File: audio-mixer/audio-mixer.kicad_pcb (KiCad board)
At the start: 2 copper layers, 72.5 x 151.2 mm, 57 parts, among them J1 Input A1, J10 Pot, J11 Input B3, J12 Pot, J13 Pot, J14 Output A, J15 Pot, J16 Output B, J17 AudioJack4, J18 Power, J19 Power, J2 Pot, J20 Power, J3 Input A2, J4 Pot, J5 Input A3, J6 Pot, J7 Input B1, J8 Pot, J9 Input B2, SW1 Mono/Stereo, U1 TL074

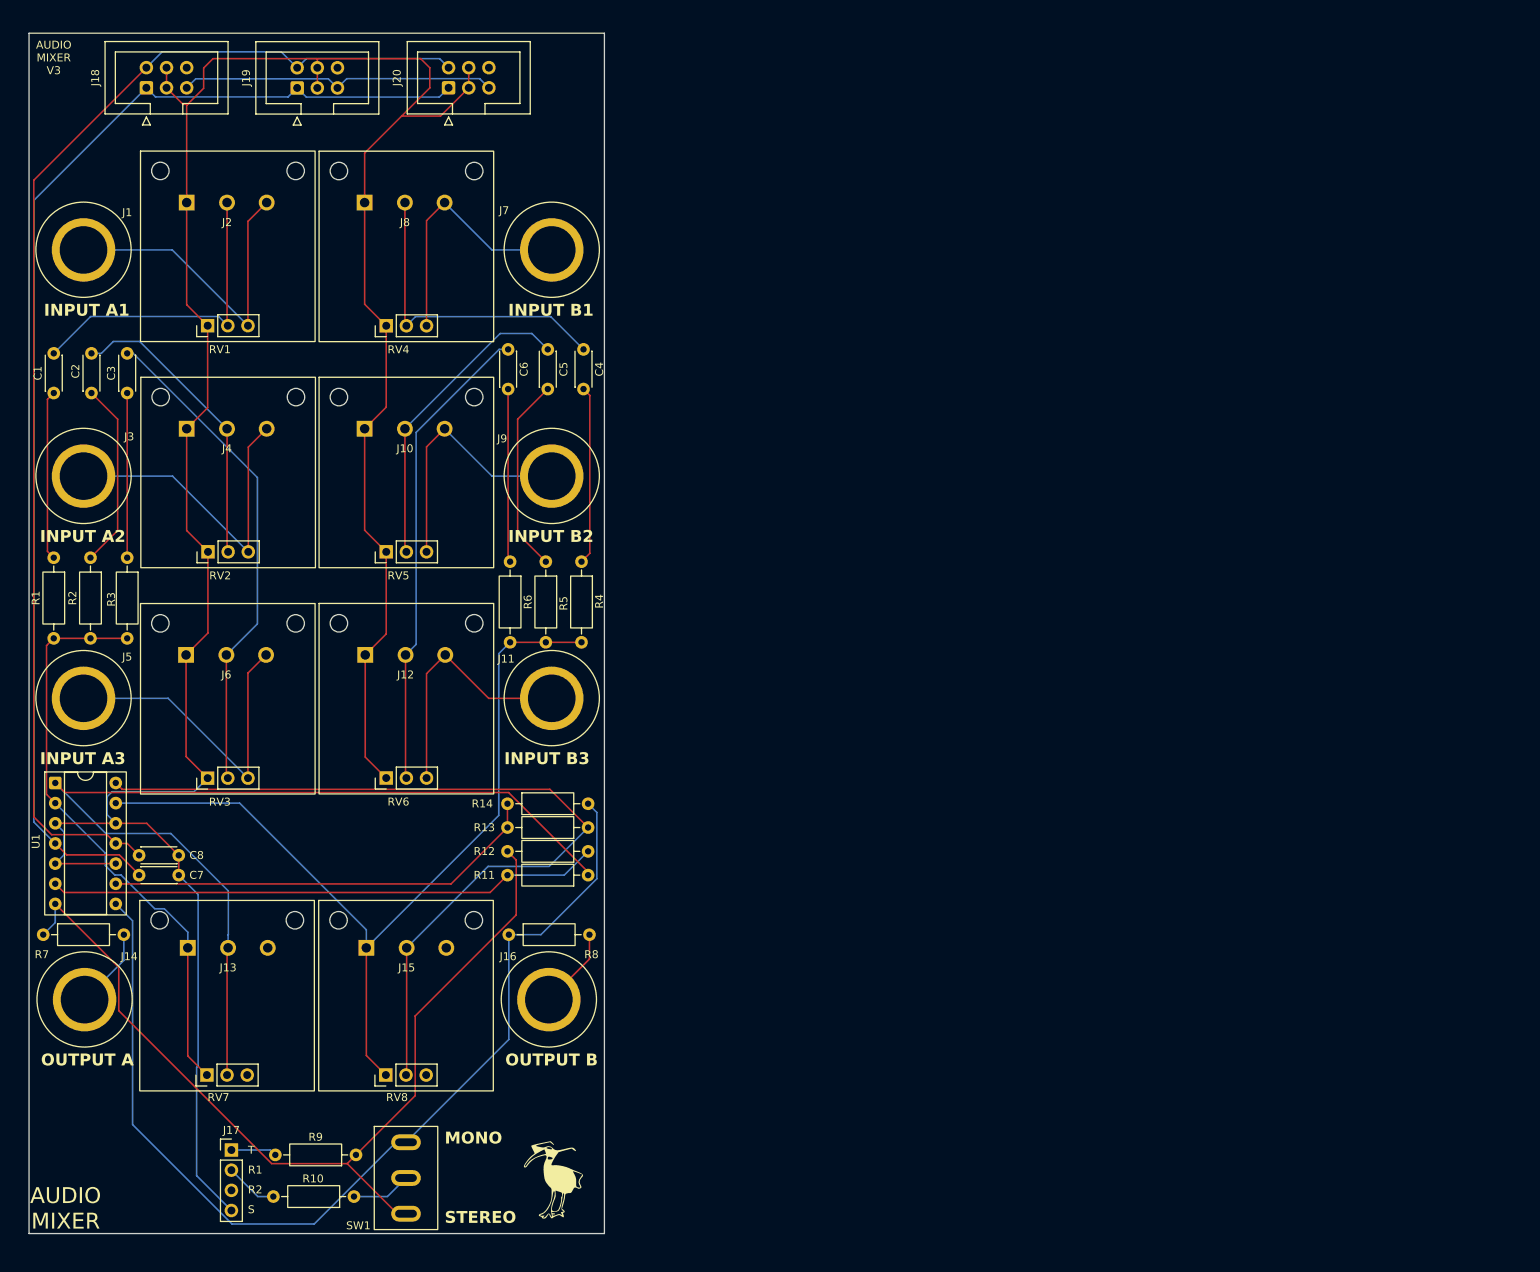
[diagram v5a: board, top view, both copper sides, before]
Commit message: Update audio mixer to new format
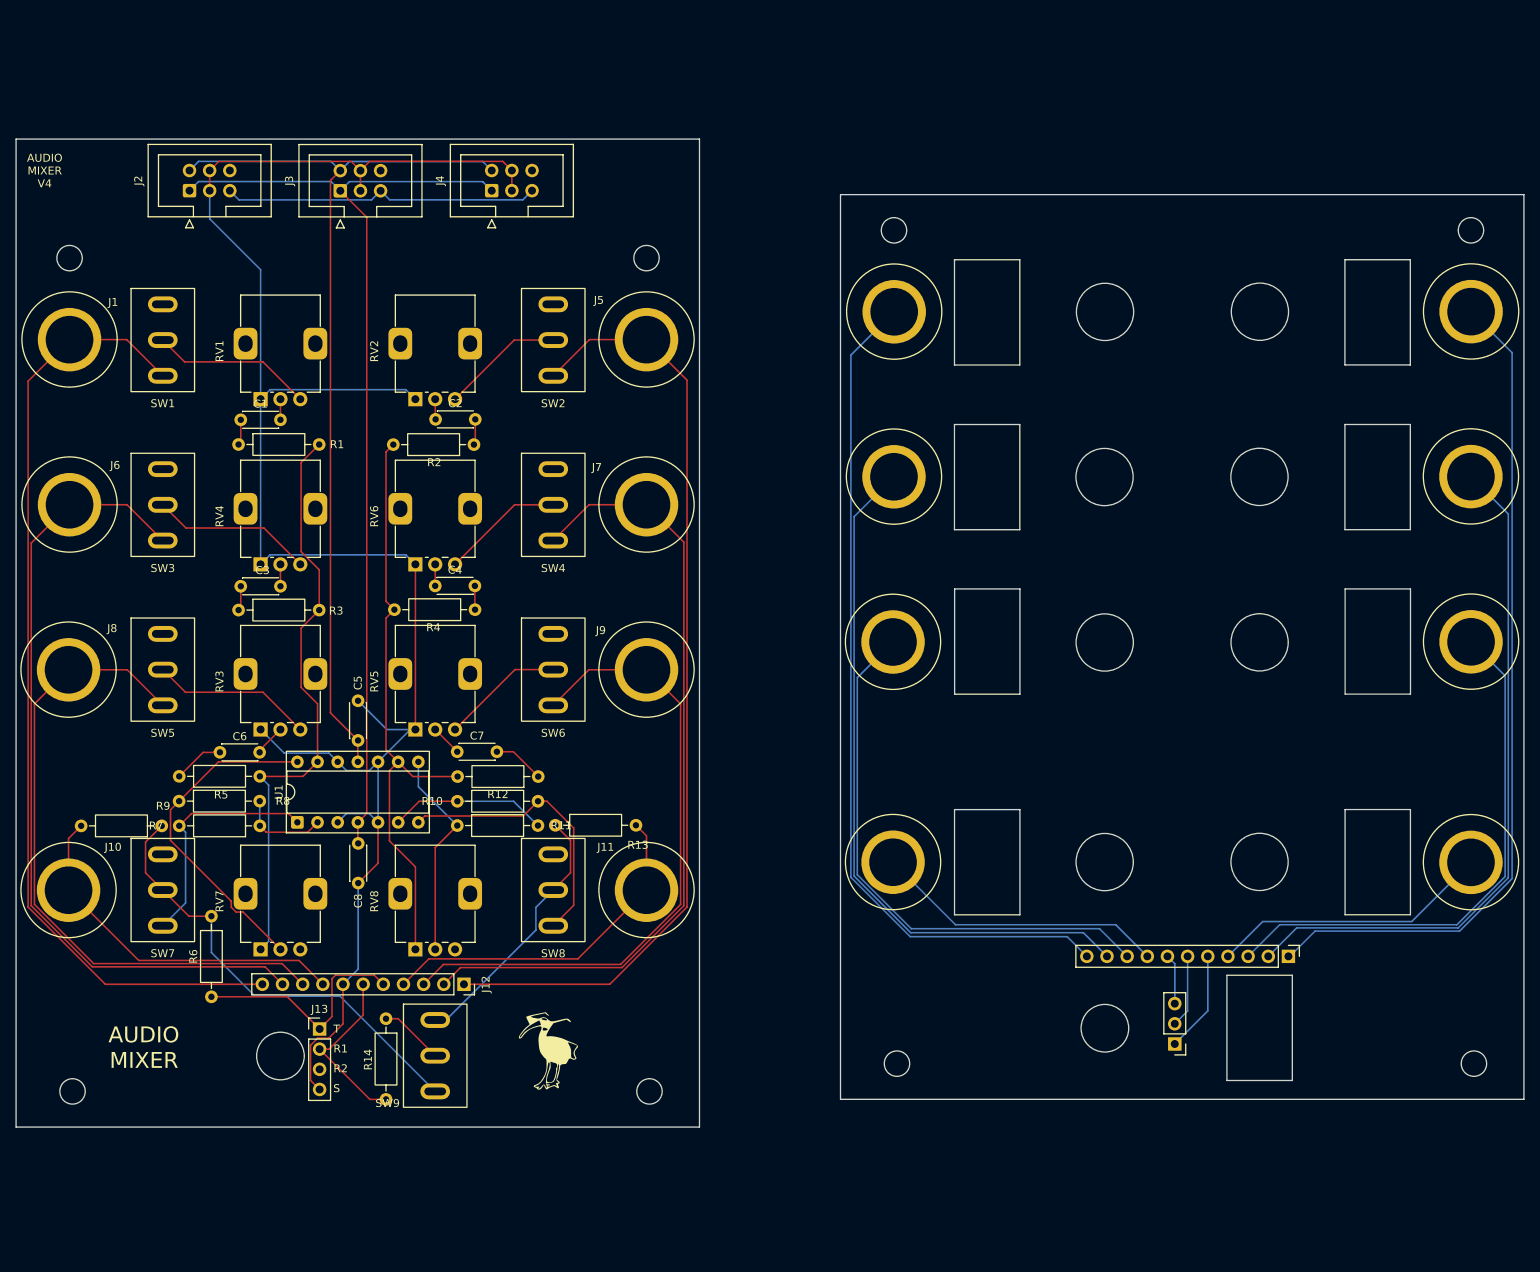
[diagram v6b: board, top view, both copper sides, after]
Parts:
- removed F1, F2, F3, F4: foot, modular2:foot
- removed the J10 at (78.0, 77.5)
- removed the J13 at (55.7, 142.9)
- removed the J2 at (55.6, 49.0)
- removed the J4 at (55.6, 77.5)
- removed the J6 at (55.5, 106.0)
- removed the J8 at (78.0, 49.0)
- added J14: Input A1, modular2:banana-jack, F.Cu at (139.7, 59.7)
- added J16: Input A2, modular2:banana-jack, F.Cu at (139.6, 80.5)
- added J17: Input B2, modular2:banana-jack, F.Cu at (212.3, 80.5)
- added J18: Input A3, modular2:banana-jack, F.Cu at (139.5, 101.3)
- added J19: Input B3, modular2:banana-jack, F.Cu at (212.3, 101.3)
- added J20: Output A, modular2:banana-jack, F.Cu at (139.5, 129.1)
- added J21: Output B, modular2:banana-jack, F.Cu at (212.3, 129.1)
- added J22: Conn_01x11_Pin, Connector_PinHeader_2.54mm:PinHeader_1x11_P2.54mm_Vertical, F.Cu at (189.3, 141.0)
- added J23: Conn_01x03_Pin, Connector_PinHeader_2.54mm:PinHeader_1x03_P2.54mm_Vertical, F.Cu at (175.0, 152.0)
- added REF**: MountingHole_3.2mm_M3, MountingHole:MountingHole_3.2mm_M3, F.Cu at (108.8, 158.0)
- added REF**: MountingHole_3.2mm_M3, MountingHole:MountingHole_3.2mm_M3, F.Cu at (139.6, 49.5)
- added REF**: MountingHole_3.2mm_M3, MountingHole:MountingHole_3.2mm_M3, F.Cu at (212.3, 49.5)
- added REF**: MountingHole_3.2mm_M3, MountingHole:MountingHole_3.2mm_M3, F.Cu at (35.7, 53.0)
- added REF**: MountingHole_3.2mm_M3, MountingHole:MountingHole_3.2mm_M3, F.Cu at (140.0, 154.5)
- added REF**: MountingHole_3.2mm_M3, MountingHole:MountingHole_3.2mm_M3, F.Cu at (108.4, 53.0)
- added REF**: MountingHole_3.2mm_M3, MountingHole:MountingHole_3.2mm_M3, F.Cu at (212.7, 154.5)
- added REF**: MountingHole_3.2mm_M3, MountingHole:MountingHole_3.2mm_M3, F.Cu at (36.1, 158.0)
- added SW1: Iso A1, modular2:switch1, F.Cu at (47.5, 63.3)
- added SW2: Iso B1, modular2:switch1, F.Cu at (96.7, 63.3)
- added SW3: Iso A2, modular2:switch1, F.Cu at (47.5, 84.1)
- added SW4: Iso B2, modular2:switch1, F.Cu at (96.7, 84.1)
- added SW5: Iso A3, modular2:switch1, F.Cu at (47.5, 104.8)
- added SW6: Iso B3, modular2:switch1, F.Cu at (96.7, 104.8)
- added SW7: Iso A, modular2:switch1, F.Cu at (47.5, 132.6)
- added SW8: Iso B, modular2:switch1, F.Cu at (96.7, 132.6)
- J12: value Pot -> Conn_01x11_Socket; footprint modular2:pot -> Connector_PinSocket_2.54mm:PinSocket_1x11_P2.54mm_Vertical
- J15: value Pot -> Input B1; footprint modular2:pot -> modular2:banana-jack
- RV1: value 100K -> 100K - A1; footprint modular2:pot-socket -> modular2:Potentiometer_Alps_RK09K_Single_Vertical - knob padding
- RV2: renamed from RV4; value 100K -> 100K - B1; footprint modular2:pot-socket -> modular2:Potentiometer_Alps_RK09K_Single_Vertical - knob padding
- RV3: value 100K -> 100K - A3; footprint modular2:pot-socket -> modular2:Potentiometer_Alps_RK09K_Single_Vertical - knob padding
- RV4: renamed from RV2; value 100K -> 100K - A2; footprint modular2:pot-socket -> modular2:Potentiometer_Alps_RK09K_Single_Vertical - knob padding
- RV5: renamed from RV6; value 100K -> 100K - B3; footprint modular2:pot-socket -> modular2:Potentiometer_Alps_RK09K_Single_Vertical - knob padding
- RV6: renamed from RV5; value 100K -> 100K - B2; footprint modular2:pot-socket -> modular2:Potentiometer_Alps_RK09K_Single_Vertical - knob padding
- RV7: value 100K -> 100K - A; footprint modular2:pot-socket -> modular2:Potentiometer_Alps_RK09K_Single_Vertical - knob padding
- RV8: value 100K -> 100K - B; footprint modular2:pot-socket -> modular2:Potentiometer_Alps_RK09K_Single_Vertical - knob padding
- moved J15 157.8 mm to (212.3, 59.7)
- moved C6 53.0 mm to (59.7, 115.3), turned to 180 degrees
- moved R8 52.4 mm to (49.5, 121.4), turned to 0 degrees
- moved C7 51.1 mm to (84.6, 115.2), turned to 0 degrees
- moved R7 41.5 mm to (59.7, 124.5)
- moved J12 39.2 mm to (85.4, 144.5), turned to -90 degrees
- moved C3 37.8 mm to (62.3, 94.3), turned to 180 degrees
- moved R6 35.2 mm to (53.6, 135.9), turned to -90 degrees
- moved C4 33.0 mm to (81.8, 94.3), turned to 0 degrees
- moved U1 30.9 mm to (64.4, 124.1), turned to 90 degrees
- moved C5 29.8 mm to (72.1, 108.8), turned to -90 degrees
- moved C1 29.8 mm to (62.3, 73.4), turned to 180 degrees
- moved R5 28.3 mm to (49.6, 118.3), turned to 0 degrees
- moved R1 27.3 mm to (57.0, 76.5), turned to 0 degrees
- moved R12 27.3 mm to (94.8, 118.3), turned to 180 degrees
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- renumbered C4 to C2, C2 to C3, C5 to C4, C8 to C5, C3 to C6, C6 to C7, C7 to C8, J14 to J10, J16 to J11, J17 to J13, J18 to J2, J19 to J3, J20 to J4, J7 to J5, J3 to J6, J9 to J7, J5 to J8, J11 to J9, R14 to R10, R13 to R11, R6 to R12, R8 to R13, R10 to R14, R4 to R2, R2 to R3, R5 to R4, R3 to R5, R9 to R6, R12 to R7, R11 to R8, R7 to R9, SW1 to SW9
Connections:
- C7 pad 1: Net-(J12-Pin_2) -> Net-(C7-Pad1)
- J10 pad 1: Net-(J14-Pin_1) -> Net-(J10-Pin_1)
- J11 pad 1: Net-(J16-Pin_1) -> Net-(J11-Pin_1)
- J12 pad 1: GND -> Net-(J12-Pin_1)
- J12 pad 3: Net-(J11-Pin_1) -> Net-(J12-Pin_3)
- J13 pad R1: Net-(J17-PadR1) -> Net-(J12-Pin_6)
- J13 pad T: Net-(J17-PadT) -> Net-(J12-Pin_5)
- J5 pad 1: Net-(J7-Pin_1) -> Net-(J12-Pin_1)
- J6 pad 1: Net-(J3-Pin_1) -> Net-(J12-Pin_10)
- J7 pad 1: Net-(J10-Pin_3) -> Net-(J12-Pin_2)
- J8 pad 1: Net-(J5-Pin_1) -> Net-(J12-Pin_9)
- J9 pad 1: Net-(J11-Pin_1) -> Net-(J12-Pin_3)
- R1 pad 2: Net-(J13-Pin_1) -> Net-(U1D--)
- R10 pad 1: Net-(U1C--) -> Net-(U1B--)
- R10 pad 2: Net-(SW1-A) -> Net-(SW8-C)
- R11 pad 1: Net-(J15-Pin_2) -> Net-(R11-Pad1)
- R11 pad 2: Net-(U1C--) -> Net-(U1B--)
- R12 pad 2: Net-(J15-Pin_1) -> Net-(U1C--)
- R13 pad 1: Net-(SW1-A) -> Net-(SW8-B)
- R13 pad 2: Net-(J16-Pin_1) -> Net-(J11-Pin_1)
- R14 pad 2: Net-(J17-PadR1) -> Net-(J12-Pin_6)
- R2 pad 2: Net-(J15-Pin_1) -> Net-(U1C--)
- R3 pad 2: Net-(J13-Pin_1) -> Net-(U1D--)
- R4 pad 2: Net-(J15-Pin_1) -> Net-(U1C--)
- R5 pad 2: Net-(J13-Pin_1) -> Net-(U1D--)
- R6 pad 1: Net-(SW1-C) -> Net-(SW7-B)
- R6 pad 2: Net-(J17-PadT) -> Net-(J12-Pin_5)
- R7 pad 1: Net-(U1B--) -> Net-(U1A--)
- R7 pad 2: Net-(SW1-C) -> Net-(SW7-C)
- R8 pad 1: Net-(J13-Pin_2) -> Net-(R8-Pad1)
- R8 pad 2: Net-(U1B--) -> Net-(U1A--)
- R9 pad 1: Net-(SW1-C) -> Net-(SW7-B)
- R9 pad 2: Net-(J14-Pin_1) -> Net-(J10-Pin_1)
- RV1 pad 3: Net-(J1-Pin_1) -> Net-(SW1-B)
- RV2 pad 3: Net-(J7-Pin_1) -> Net-(SW2-B)
- RV3 pad 3: Net-(J5-Pin_1) -> Net-(SW5-B)
- RV4 pad 3: Net-(J3-Pin_1) -> Net-(SW3-B)
- RV5 pad 2: Net-(J12-Pin_2) -> Net-(C7-Pad1)
- RV5 pad 3: Net-(J11-Pin_1) -> Net-(SW6-B)
- RV6 pad 3: Net-(J10-Pin_3) -> Net-(SW4-B)
- RV7 pad 1: Net-(J13-Pin_1) -> Net-(U1D--)
- RV7 pad 2: Net-(J13-Pin_2) -> Net-(R8-Pad1)
- RV8 pad 1: Net-(J15-Pin_1) -> Net-(U1C--)
- RV8 pad 2: Net-(J15-Pin_2) -> Net-(R11-Pad1)
- SW9 pad 1: Net-(SW1-C) -> Net-(SW7-B)
- SW9 pad 3: Net-(SW1-A) -> Net-(SW8-B)
- U1 pad 1: Net-(J13-Pin_2) -> Net-(SW7-C)
- U1 pad 13: Net-(J15-Pin_1) -> Net-(U1D--)
- U1 pad 14: Net-(J15-Pin_2) -> Net-(R8-Pad1)
- U1 pad 2: Net-(J13-Pin_1) -> Net-(U1A--)
- U1 pad 7: Net-(SW1-C) -> Net-(SW8-C)
- U1 pad 8: Net-(SW1-A) -> Net-(R11-Pad1)
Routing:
- net Net-(SW1-A): track 128.0 -> 0.00 mm
- net Net-(J13-Pin_2): track 122.9 -> 0.00 mm
- net Net-(J12-Pin_1): track 0.00 -> 119.4 mm
- net Net-(SW1-C): track 116.7 -> 0.00 mm
- net Net-(J15-Pin_2): track 107.0 -> 0.00 mm
- net Net-(J12-Pin_10): track 0.00 -> 101.9 mm
- net GND: track 342.0 -> 243.8 mm
- net Net-(J14-Pin_1): track 10.2 -> 107.4 mm
- net Net-(J17-Pin_1): track 0.00 -> 86.9 mm
- net Net-(J12-Pin_9): track 0.00 -> 83.0 mm
- net Net-(J12-Pin_3): track 0.00 -> 81.5 mm
- net Net-(J1-Pin_1): track 41.2 -> 120.8 mm
- net Net-(J16-Pin_1): track 10.3 -> 88.4 mm
- net Net-(U1D--): track 0.00 -> 74.4 mm
- net Net-(J13-Pin_1): track 74.2 -> 0.00 mm
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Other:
- board size 72.5 x 151.2 mm -> 190 x 124.5 mm
- board text added: "AUDIO MIXER V4"
- board text removed: "AUDIO MIXER V3"
- board text removed: "INPUT A1"
- board text removed: "INPUT A2"
- board text removed: "INPUT A3"
- board text removed: "INPUT B1"
- board text removed: "INPUT B2"
- board text removed: "INPUT B3"
- board text removed: "MONO"
- board text removed: "OUTPUT A"
- board text removed: "OUTPUT B"
- board text removed: "STEREO"
